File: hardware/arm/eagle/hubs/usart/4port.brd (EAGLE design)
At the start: 24.3 x 30.9 mm, 15 parts

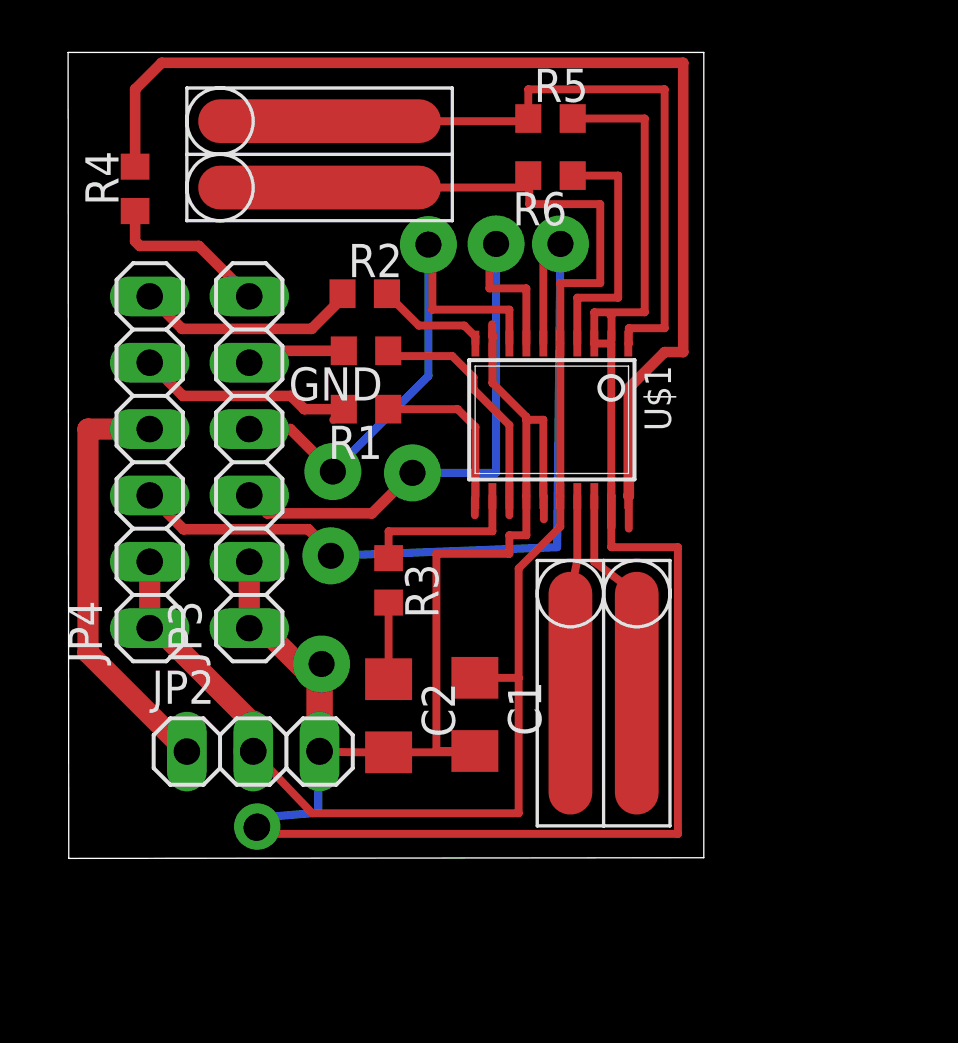
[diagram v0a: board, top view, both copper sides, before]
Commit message: updated uart hub pcb
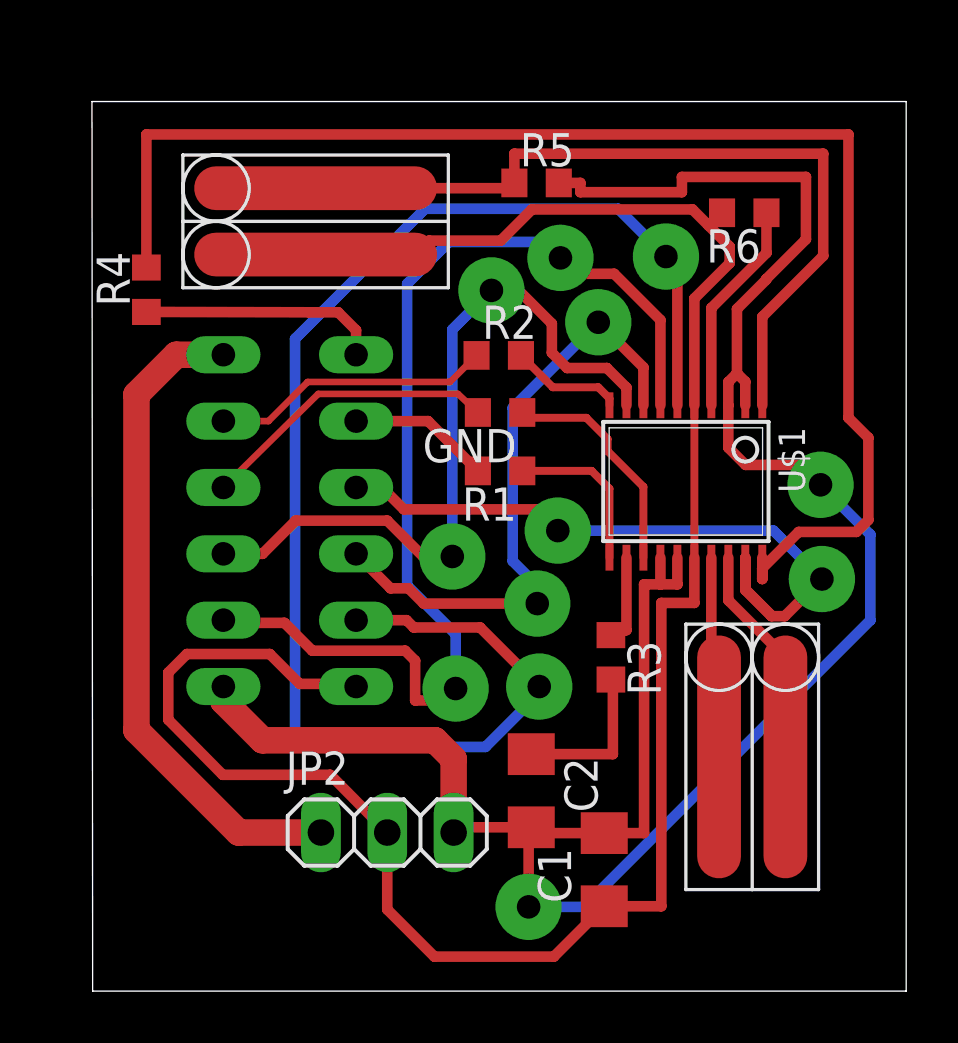
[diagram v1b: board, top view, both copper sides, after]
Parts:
- removed JP3, JP4: (no value), pinhead:1X06
- added U$4: HUB_PORT, gumyns:HUB_PORT
- moved R3 9.00 mm to (20.0, 12.5)
- moved C1 7.74 mm to (19.8, 4.37), turned to 90 degrees
- moved R6 7.55 mm to (25.1, 29.5)
- moved U$3 6.19 mm to (25.5, 13.8)
- moved C2 6.17 mm to (17.0, 7.39)
- moved JP2 5.99 mm to (11.5, 5.79)
- moved GND 5.65 mm to (15.8, 21.9)
- moved R1 5.65 mm to (15.8, 19.6)
- moved R2 5.65 mm to (15.7, 24.1)
- moved U$1 5.65 mm to (22.9, 19.2)
- moved R4 3.88 mm to (2.26, 26.6)
- moved U$2 2.57 mm to (3.66, 29.2)
- moved R5 2.52 mm to (17.2, 30.7)
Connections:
- removed net N$34: JP4.1
- new net E: U$1.19, U$4.E
- net 12V: now also U$4.12V; no longer JP4.4
- net 3.3V: now also U$4.3.3V; no longer JP4.2
- net A: now also U$4.A; no longer JP4.3
- net B: now also U$4.B; no longer JP3.3
- net C: now also U$4.C; no longer JP3.4
- net D: now also U$1.9, U$4.D; no longer JP3.1
- net DATA: now also U$4.DATA; no longer JP3.5
- net GND: now also U$4.GND; no longer JP3.2, U$1.19, U$1.9
- net INT: now also U$4.INT; no longer JP3.6
- net NSS: now also U$4.NSS; no longer JP4.6
- net SCK: now also U$4.SCK; no longer JP4.5
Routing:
- net D: track 0.00 -> 28.7 mm, vias 0 -> 2
- net E: track 0.00 -> 27.1 mm, vias 0 -> 2
- net A: track 32.5 -> 56.9 mm
- net 3.3V: track 55.7 -> 76.1 mm, vias 1 -> 0
- net B: track 24.5 -> 42.4 mm
- net GND: track 98.8 -> 87.6 mm, vias 3 -> 2
- net N$28: track 42.2 -> 53.1 mm
- net 12V: track 16.3 -> 25.5 mm
- net DATA: track 3.81 -> 11.5 mm
- net N$14: track 21.7 -> 27.5 mm
- net SCK: track 8.74 -> 5.45 mm
- net C: track 20.9 -> 24.1 mm
- net N$1: track 2.93 -> 6.00 mm
- net N$6: track 6.35 -> 3.40 mm
- net INT: track 6.40 -> 9.25 mm
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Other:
- board size 24.3 x 30.9 mm -> 31.2 x 34.1 mm
